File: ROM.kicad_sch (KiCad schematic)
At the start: 1 part, among them U7 74AHC595

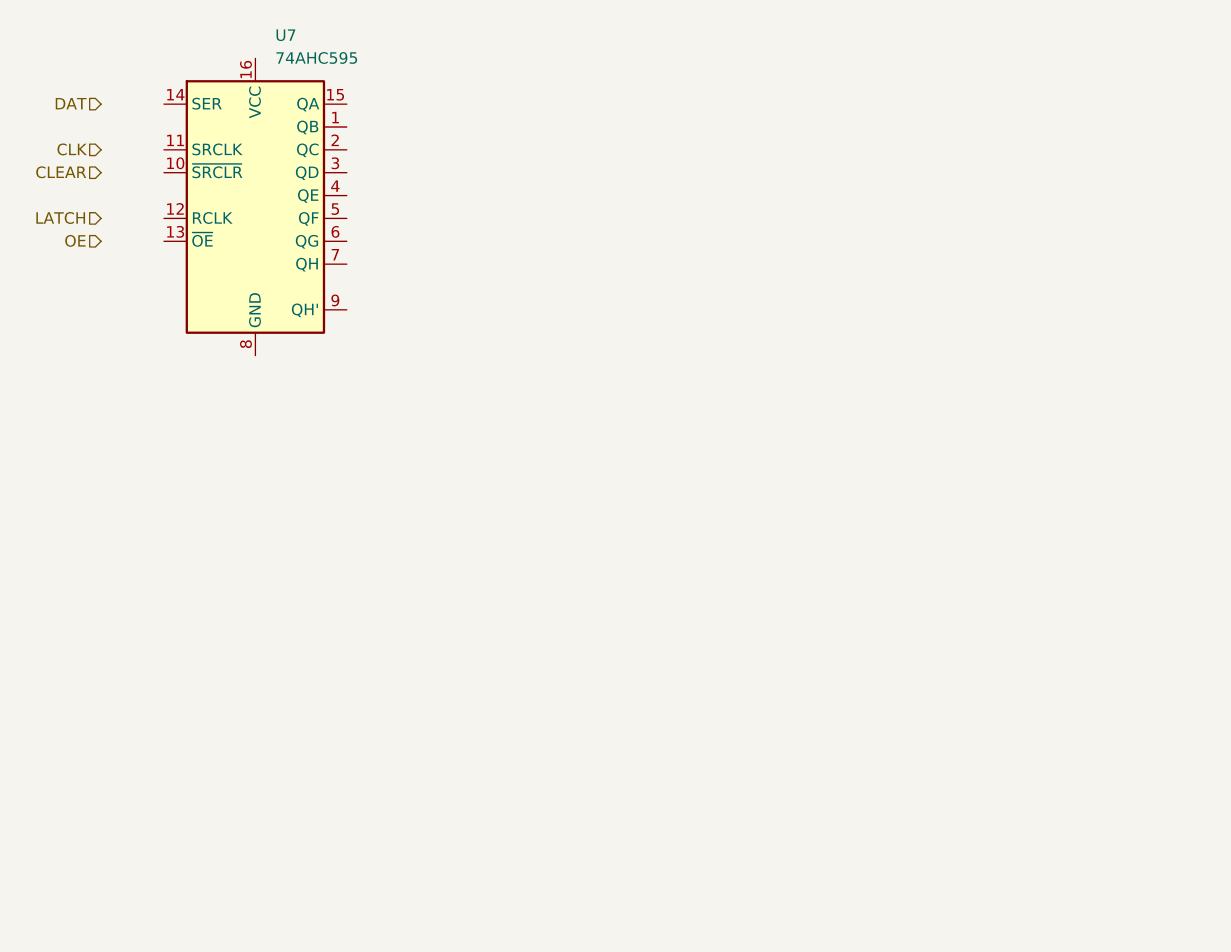
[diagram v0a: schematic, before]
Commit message: Begin screen module
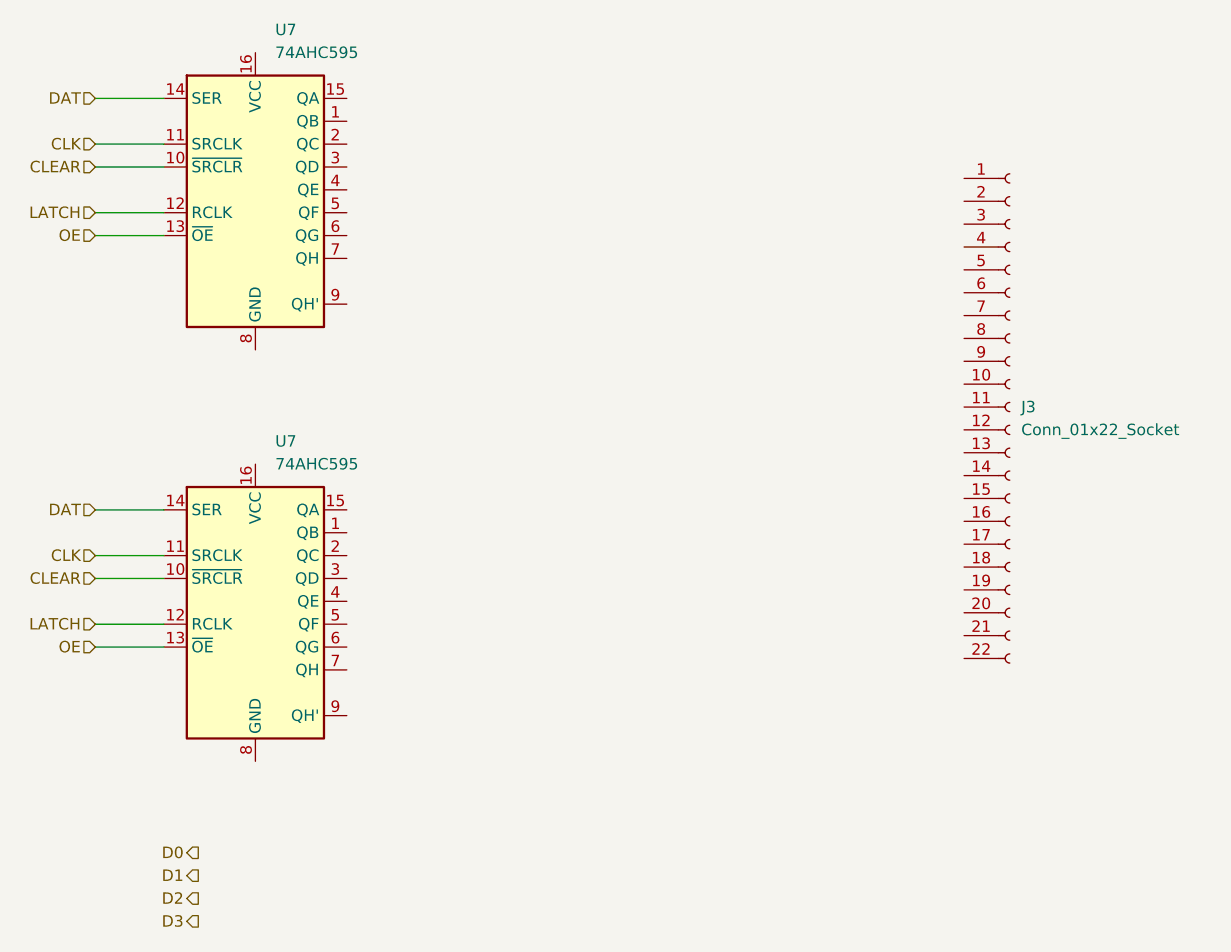
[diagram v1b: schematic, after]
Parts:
- added J3: Conn_01x22_Socket, symbol Connector:Conn_01x22_Socket
- added U7: 74AHC595, symbol 74xx:74AHC595
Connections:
- net CLEAR: now also U7.10 (~{SRCLR}), U7.10 (~{SRCLR})
- net CLK: now also U7.11 (SRCLK), U7.11 (SRCLK)
- net DAT: now also U7.14 (SER), U7.14 (SER)
- net LATCH: now also U7.12 (RCLK), U7.12 (RCLK)
- net OE: now also U7.13 (~{OE}), U7.13 (~{OE})
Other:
- moved on the sheet: U7
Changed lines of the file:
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@@
-(kicad_sch (version 20230121) (generator eeschema)
+(kicad_sch (version 20230819) (generator eeschema)
   (paper "A4")
-  (hierarchical_label "DAT" (shape input) (at 85.725 38.735 180) (fields_autoplaced)
-    (effects (font (size 1.27 1.27)) (justify right))
-  )
-  (hierarchical_label "OE" (shape input) (at 85.725 53.975 180) (fields_autoplaced)
-    (effects (font (size 1.27 1.27)) (justify right))
-  )
-  (hierarchical_label "CLK" (shape input) (at 85.725 43.815 180) (fields_autoplaced)
-    (effects (font (size 1.27 1.27)) (justify right))
-  )
-  (hierarchical_label "CLEAR" (shape input) (at 85.725 46.355 180) (fields_autoplaced)
-    (effects (font (size 1.27 1.27)) (justify right))
-  )
-  (hierarchical_label "LATCH" (shape input) (at 85.725 51.435 180) (fields_autoplaced)
-    (effects (font (size 1.27 1.27)) (justify right))
-  )
-  (symbol (lib_id "74xx:74AHC595") (at 102.87 48.895 0) (unit 1)
-    (in_bom yes) (on_board yes) (dnp no) (fields_autoplaced)
-    (property "Reference" "U7" (at 105.0641 31.115 0)
-      (effects (font (size 1.27 1.27)) (justify left))
-    )
-    (property "Value" "74AHC595" (at 105.0641 33.655 0)
-      (effects (font (size 1.27 1.27)) (justify left))
-    )
-    (property "Footprint" "" (at 102.87 48.895 0)
-      (effects (font (size 1.27 1.27)) hide)
-    )
-    (property "Datasheet" "https://assets.nexperia.com/documents/data-sheet/74AHC_AHCT595.pdf" (at 102.87 48.895 0)
+  (wire (pts (xy 85.09 45.72) (xy 92.71 45.72))
+    (stroke (width 0) (type default))
+  )
+  (wire (pts (xy 85.09 53.34) (xy 92.71 53.34))
+    (stroke (width 0) (type default))
+  )
+  (wire (pts (xy 85.09 91.44) (xy 92.71 91.44))
+    (stroke (width 0) (type default))
+  )
+  (wire (pts (xy 85.09 50.8) (xy 92.71 50.8))
+    (stroke (width 0) (type default))
+  )
+  (wire (pts (xy 85.09 38.1) (xy 92.71 38.1))
+    (stroke (width 0) (type default))
+  )
+  (wire (pts (xy 85.09 43.18) (xy 92.71 43.18))
+    (stroke (width 0) (type default))
+  )
+  (wire (pts (xy 85.09 96.52) (xy 92.71 96.52))
+    (stroke (width 0) (type default))
+  )
+  (wire (pts (xy 85.09 88.9) (xy 92.71 88.9))
+    (stroke (width 0) (type default))
+  )
+  (wire (pts (xy 85.09 83.82) (xy 92.71 83.82))
+    (stroke (width 0) (type default))
+  )
+  (wire (pts (xy 85.09 99.06) (xy 92.71 99.06))
+    (stroke (width 0) (type default))
+  )
+  (hierarchical_label "OE" (shape input) (at 85.09 99.06 180) (fields_autoplaced)
+    (effects (font (size 1.27 1.27)) (justify right))
+  )
+  (hierarchical_label "DAT" (shape input) (at 85.09 38.1 180) (fields_autoplaced)
+    (effects (font (size 1.27 1.27)) (justify right))
+  )
+  (hierarchical_label "D1" (shape output) (at 96.52 124.46 180) (fields_autoplaced)
+    (effects (font (size 1.27 1.27)) (justify right))
+  )
+  (hierarchical_label "OE" (shape input) (at 85.09 53.34 180) (fields_autoplaced)
+    (effects (font (size 1.27 1.27)) (justify right))
+  )
+  (hierarchical_label "LATCH" (shape input) (at 85.09 96.52 180) (fields_autoplaced)
+    (effects (font (size 1.27 1.27)) (justify right))
+  )
+  (hierarchical_label "CLK" (shape input) (at 85.09 88.9 180) (fields_autoplaced)
+    (effects (font (size 1.27 1.27)) (justify right))
+  )
+  (hierarchical_label "DAT" (shape input) (at 85.09 83.82 180) (fields_autoplaced)
+    (effects (font (size 1.27 1.27)) (justify right))
+  )
+  (hierarchical_label "CLK" (shape input) (at 85.09 43.18 180) (fields_autoplaced)
+    (effects (font (size 1.27 1.27)) (justify right))
+  )
+  (hierarchical_label "D0" (shape output) (at 96.52 121.92 180) (fields_autoplaced)
+    (effects (font (size 1.27 1.27)) (justify right))
+  )
+  (hierarchical_label "D2" (shape output) (at 96.52 127 180) (fields_autoplaced)
+    (effects (font (size 1.27 1.27)) (justify right))
+  )
+  (hierarchical_label "D3" (shape output) (at 96.52 129.54 180) (fields_autoplaced)
+    (effects (font (size 1.27 1.27)) (justify right))
+  )
+  (hierarchical_label "CLEAR" (shape input) (at 85.09 45.72 180) (fields_autoplaced)
+    (effects (font (size 1.27 1.27)) (justify right))
+  )
+  (hierarchical_label "LATCH" (shape input) (at 85.09 50.8 180) (fields_autoplaced)
+    (effects (font (size 1.27 1.27)) (justify right))
+  )
+  (hierarchical_label "CLEAR" (shape input) (at 85.09 91.44 180) (fields_autoplaced)
+    (effects (font (size 1.27 1.27)) (justify right))
+  )
+  (symbol (lib_id "74xx:74AHC595") (at 102.87 48.26 0) (unit 1)
+    (exclude_from_sim no) (in_bom yes) (on_board yes) (dnp no) (fields_autoplaced)
+    (property "Reference" "U7" (at 105.0641 30.48 0)
+      (effects (font (size 1.27 1.27)) (justify left))
+    )
+    (property "Value" "74AHC595" (at 105.0641 33.02 0)
+      (effects (font (size 1.27 1.27)) (justify left))
+    )
+    (property "Footprint" "" (at 102.87 48.26 0)
+      (effects (font (size 1.27 1.27)) hide)
+    )
+    (property "Datasheet" "https://assets.nexperia.com/documents/data-sheet/74AHC_AHCT595.pdf" (at 102.87 48.26 0)
+      (effects (font (size 1.27 1.27)) hide)
+    )
+    (property "Description" "" (at 102.87 48.26 0)
       (effects (font (size 1.27 1.27)) hide)
     )
@@
           (reference "U7") (unit 1)
         )
-        (path "/e7435767-0989-47f1-96a3-8a6a374116ff/1230978a-eef3-4475-8681-586f184da2b0"
-          (reference "U7") (unit 1)
-        )
         (path "/e7435767-0989-47f1-96a3-8a6a374116ff/fc53a69d-c150-48d1-8f57-fde6c7368d16"
           (reference "U11") (unit 1)
         )
       )
+    )
+  )
+  (symbol (lib_id "Connector:Conn_01x22_Socket") (at 186.69 72.39 0) (unit 1)
+    (exclude_from_sim no) (in_bom yes) (on_board yes) (dnp no) (fields_autoplaced)
+    (property "Reference" "J3" (at 187.96 72.3899 0)
+      (effects (font (size 1.27 1.27)) (justify left))
+    )
+    (property "Value" "Conn_01x22_Socket" (at 187.96 74.9299 0)
+      (effects (font (size 1.27 1.27)) (justify left))
+    )
+    (property "Footprint" "" (at 186.69 72.39 0)
+      (effects (font (size 1.27 1.27)) hide)
+    )
+    (property "Datasheet" "~" (at 186.69 72.39 0)
+      (effects (font (size 1.27 1.27)) hide)
+    )
+    (property "Description" "Generic connector, single row, 01x22, script generated" (at 186.69 72.39 0)
+      (effects (font (size 1.27 1.27)) hide)
+    )
+    (pin "8")
+    (pin "19")
+    (pin "21")
+    (pin "22")
+    (pin "17")
+    (pin "20")
+    (pin "13")
+    (pin "16")
+    (pin "18")
+    (pin "3")
+    (pin "4")
+    (pin "11")
+    (pin "5")
+    (pin "2")
+    (pin "9")
+    (pin "7")
+    (pin "1")
+    (pin "10")
+    (pin "14")
+    (pin "6")
+    (pin "12")
+    (pin "15")
+    (instances
+      (project "calculator"
+        (path "/e7435767-0989-47f1-96a3-8a6a374116ff"
+          (reference "J3") (unit 1)
+        )
+        (path "/e7435767-0989-47f1-96a3-8a6a374116ff/fc53a69d-c150-48d1-8f57-fde6c7368d16"
+          (reference "J3") (unit 1)
+        )
+      )
+    )
+  )
+  (symbol (lib_id "74xx:74AHC595") (at 102.87 93.98 0) (unit 1)
+    (exclude_from_sim no) (in_bom yes) (on_board yes) (dnp no) (fields_autoplaced)
+    (property "Reference" "U7" (at 105.0641 76.2 0)
+      (effects (font (size 1.27 1.27)) (justify left))
+    )
+    (property "Value" "74AHC595" (at 105.0641 78.74 0)
+      (effects (font (size 1.27 1.27)) (justify left))
+    )
+    (property "Footprint" "" (at 102.87 93.98 0)
+      (effects (font (size 1.27 1.27)) hide)
+    )
+    (property "Datasheet" "https://assets.nexperia.com/documents/data-sheet/74AHC_AHCT595.pdf" (at 102.87 93.98 0)
+      (effects (font (size 1.27 1.27)) hide)
+    )
+    (property "Description" "" (at 102.87 93.98 0)
+      (effects (font (size 1.27 1.27)) hide)
+    )
+    (pin "1")
+    (pin "10")
+    (pin "11")
+    (pin "12")
+    (pin "13")
+    (pin "14")
+    (pin "15")
+    (pin "16")
+    (pin "2")
+    (pin "3")
+    (pin "4")
+    (pin "5")
+    (pin "6")
+    (pin "7")
+    (pin "8")
+    (pin "9")
+    (instances
+      (project "calculator"
+        (path "/e7435767-0989-47f1-96a3-8a6a374116ff"
+          (reference "U7") (unit 1)
+        )
+        (path "/e7435767-0989-47f1-96a3-8a6a374116ff/fc53a69d-c150-48d1-8f57-fde6c7368d16"
+          (reference "U12") (unit 1)
+        )
+      )
